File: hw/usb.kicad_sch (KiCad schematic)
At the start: 38 parts, among them J201 USB_C_Receptacle_USB2.0_14P, Q201 CSD18543Q3A, U1001 LMR51430XDDCR, U1002 TPS26750SRSMR, U1003 TPD4S480RUKR, U1004 LMR51430XDDCR, U1005 TPS63700DRCR

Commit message: Checkpoint before resuming project
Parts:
- renumbered C206 to C1001, C208 to C1002, C217 to C1003, C223 to C1004, C224 to C1005, C212 to C1006, C209 to C1007, C213 to C1008, C210 to C1009, C222 to C1010, C214 to C1011, C211 to C1012, C218 to C1013, C219 to C1014, C215 to C1015, C216 to C1016, C220 to C1017, C221 to C1018, J201 to J1001, L1003 to L1001, L1001 to L1003, Q201 to Q1001, R203 to R1001, R202 to R1002, R210 to R1003, R206 to R1004, R207 to R1005, R204 to R1006, R205 to R1007, R208 to R1008, R209 to R1009, U1003 to U1001, U1005 to U1003, U1001 to U1005

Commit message: Working on multi-band BPF and switching
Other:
- company: SoftShack -> WB7NAB
- title: USB connector, ESD, power -> ${title}
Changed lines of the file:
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@@
 	(generator "eeschema")
 	(generator_version "9.0")
-	(paper "A")
+	(paper "USLetter")
 	(title_block
-		(title "USB connector, ESD, power")
-		(date "2025-03-26")
-		(company "SoftShack")
+		(title "${title}")
+		(date "2025-08-10")
+		(company "WB7NAB")
 		(comment 1 "Alan Mimms")
-		(comment 2 "WB7NAB")
 	)
 	(junction

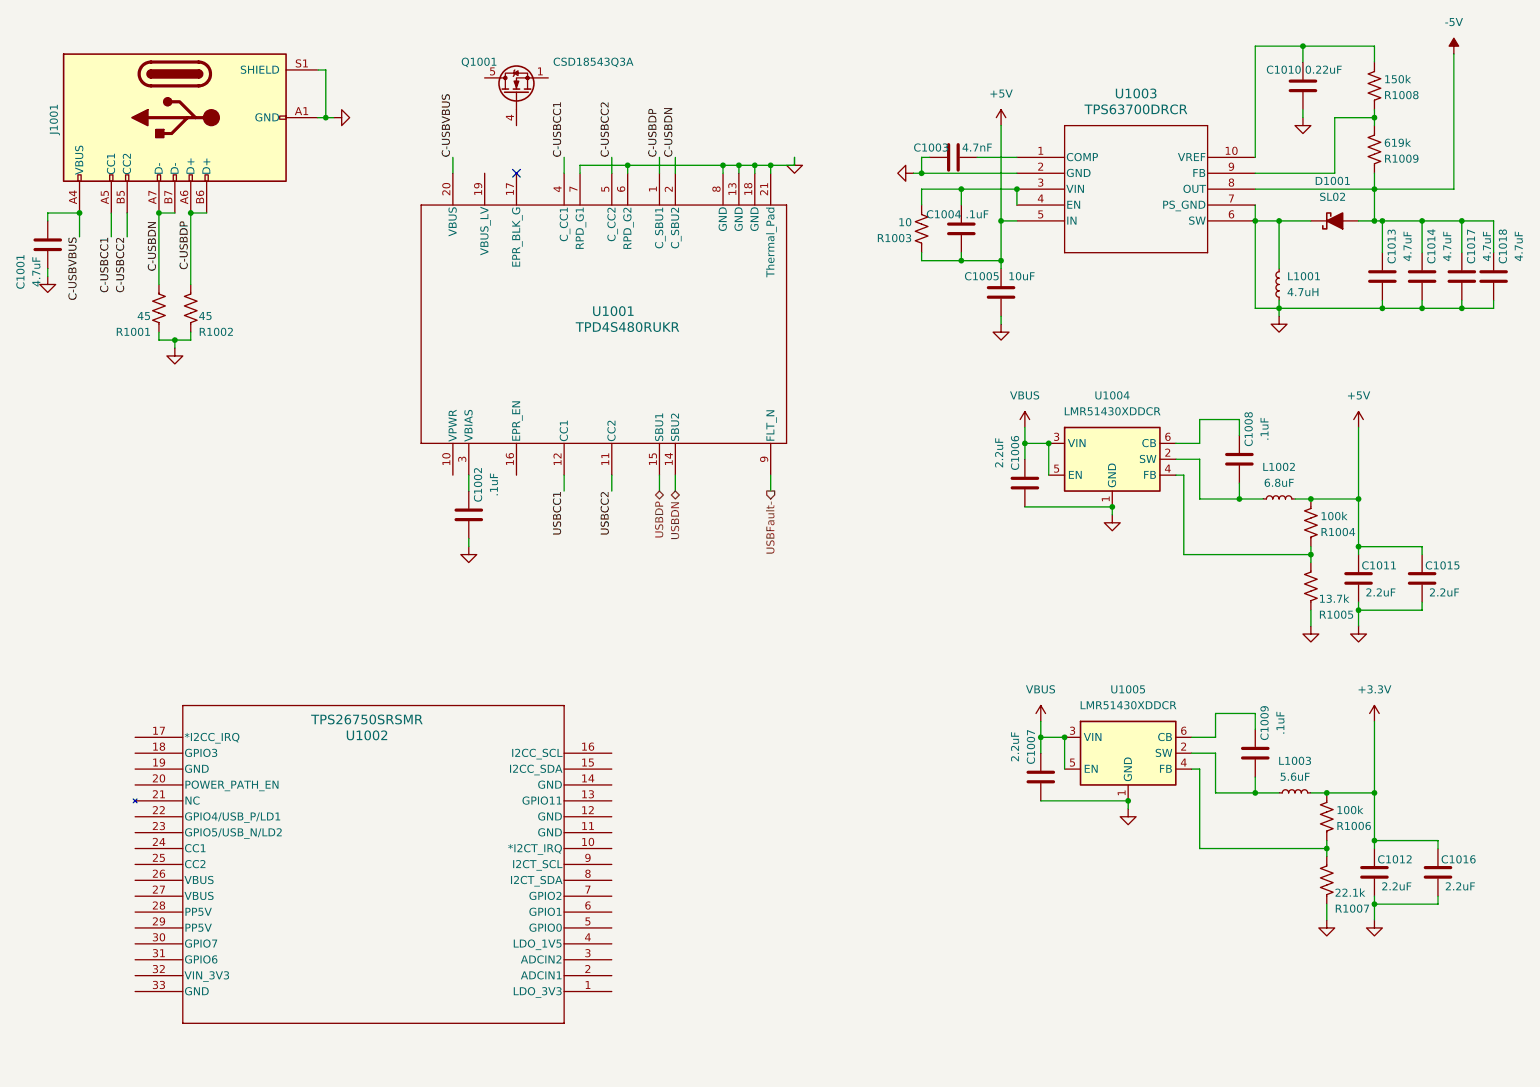
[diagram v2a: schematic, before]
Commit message: Starting to build BPFs for 7 bands
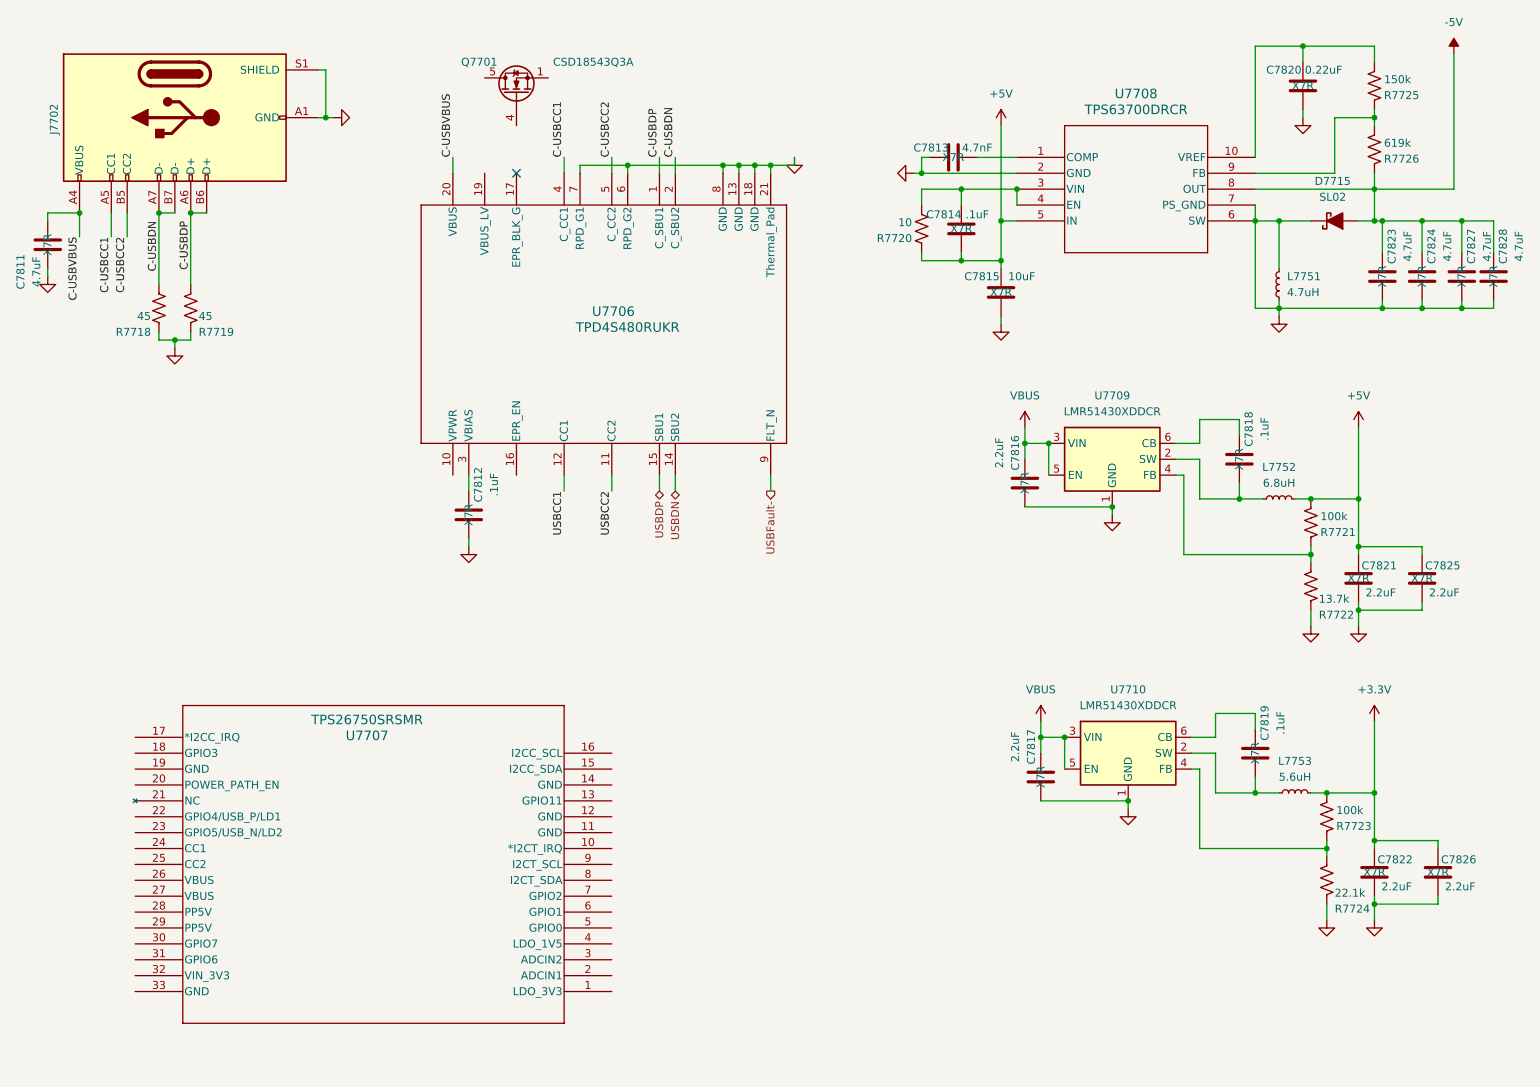
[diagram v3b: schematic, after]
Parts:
- C7811: renamed from C1001; cap-type (none) -> X7R
- C7812: renamed from C1002; cap-type (none) -> X7R
- C7813: renamed from C1003; cap-type (none) -> X7R
- C7814: renamed from C1004; cap-type (none) -> X7R
- C7815: renamed from C1005; cap-type (none) -> X7R
- C7816: renamed from C1006; cap-type (none) -> X7R
- C7817: renamed from C1007; cap-type (none) -> X7R
- C7818: renamed from C1008; cap-type (none) -> X7R
- C7819: renamed from C1009; cap-type (none) -> X7R
- C7820: renamed from C1010; cap-type (none) -> X7R
- C7821: renamed from C1011; cap-type (none) -> X7R
- C7822: renamed from C1012; cap-type (none) -> X7R
- C7823: renamed from C1013; cap-type (none) -> X7R
- C7824: renamed from C1014; cap-type (none) -> X7R
- C7825: renamed from C1015; cap-type (none) -> X7R
- C7826: renamed from C1016; cap-type (none) -> X7R
- C7827: renamed from C1017; cap-type (none) -> X7R
- C7828: renamed from C1018; cap-type (none) -> X7R
- L7752: renamed from L1002; value 6.8uF -> 6.8uH
- L7753: renamed from L1003; value 5.6uF -> 5.6uH
- renumbered D1001 to D7715, J1001 to J7702, L1001 to L7751, Q1001 to Q7701, R1001 to R7718, R1002 to R7719, R1003 to R7720, R1004 to R7721, R1005 to R7722, R1006 to R7723, R1007 to R7724, R1008 to R7725, R1009 to R7726, U1001 to U7706, U1002 to U7707, U1003 to U7708, U1004 to U7709, U1005 to U7710
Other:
- title: ${title} -> USB

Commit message: Getting closer to having all (ten) BPFs designed. Maybe I can try some layout next.
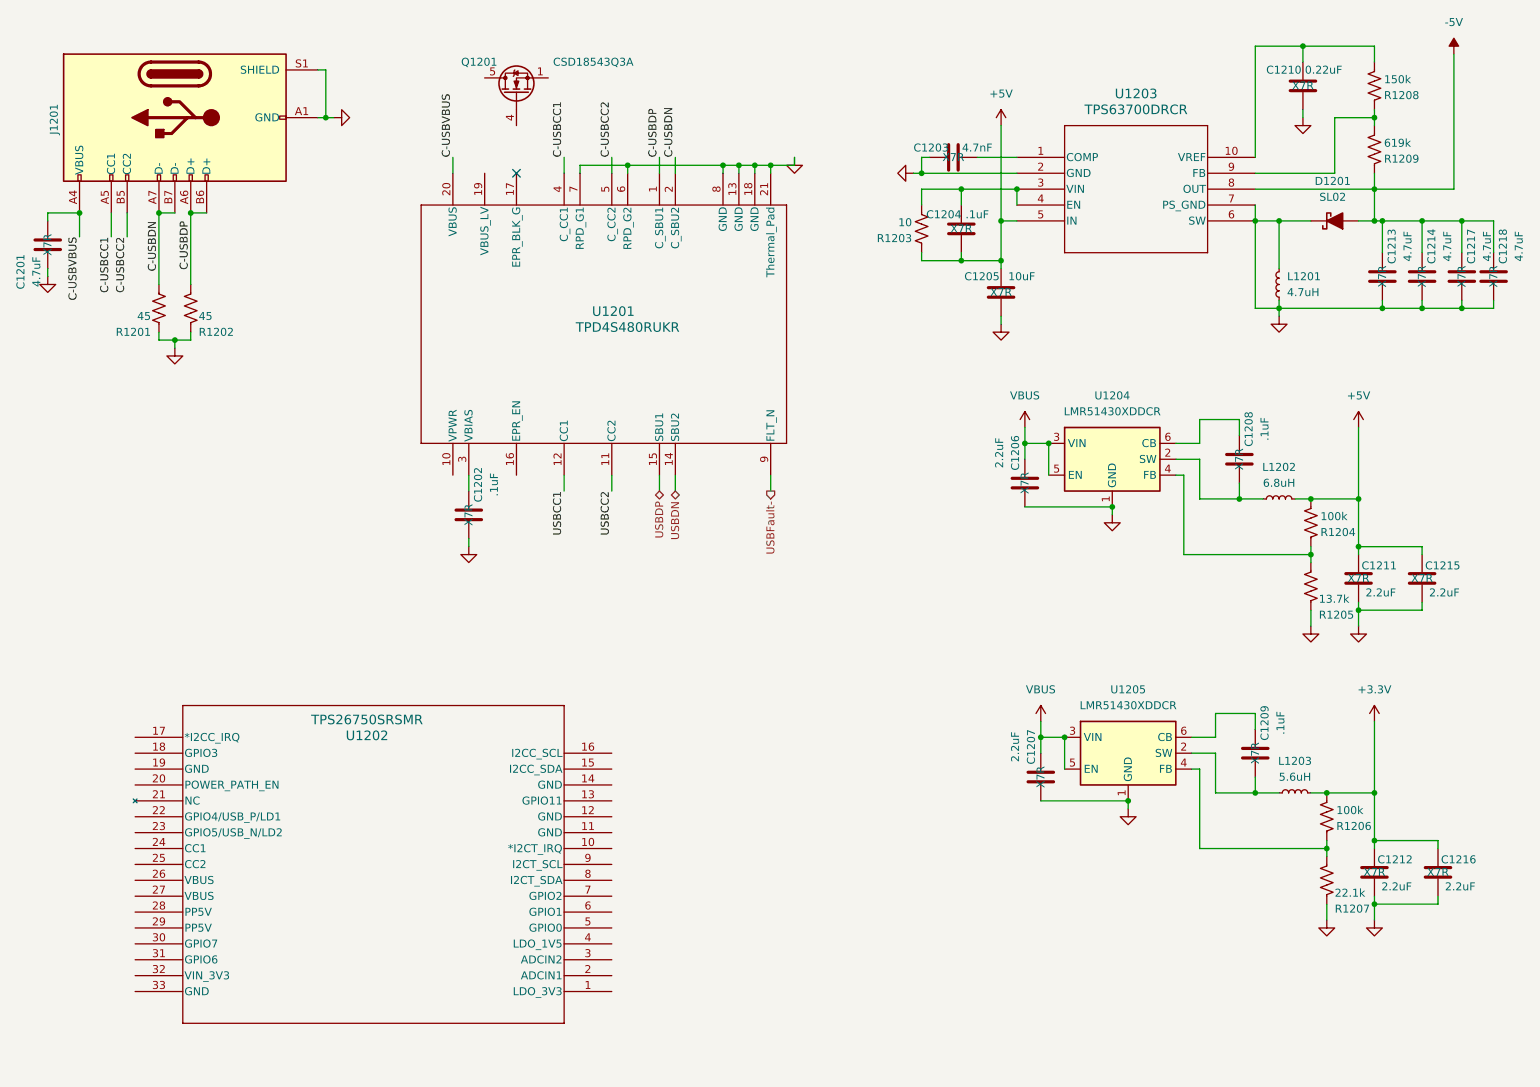
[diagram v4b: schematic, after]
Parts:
- renumbered C7811 to C1201, C7812 to C1202, C7813 to C1203, C7814 to C1204, C7815 to C1205, C7816 to C1206, C7817 to C1207, C7818 to C1208, C7819 to C1209, C7820 to C1210, C7821 to C1211, C7822 to C1212, C7823 to C1213, C7824 to C1214, C7825 to C1215, C7826 to C1216, C7827 to C1217, C7828 to C1218, D7715 to D1201, J7702 to J1201, L7751 to L1201, L7752 to L1202, L7753 to L1203, Q7701 to Q1201, R7718 to R1201, R7719 to R1202, R7720 to R1203, R7721 to R1204, R7722 to R1205, R7723 to R1206, R7724 to R1207, R7725 to R1208, R7726 to R1209, U7706 to U1201, U7707 to U1202, U7708 to U1203, U7709 to U1204, U7710 to U1205

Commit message: Checkpoint hardware. Add README with some notes about software services we need to create.
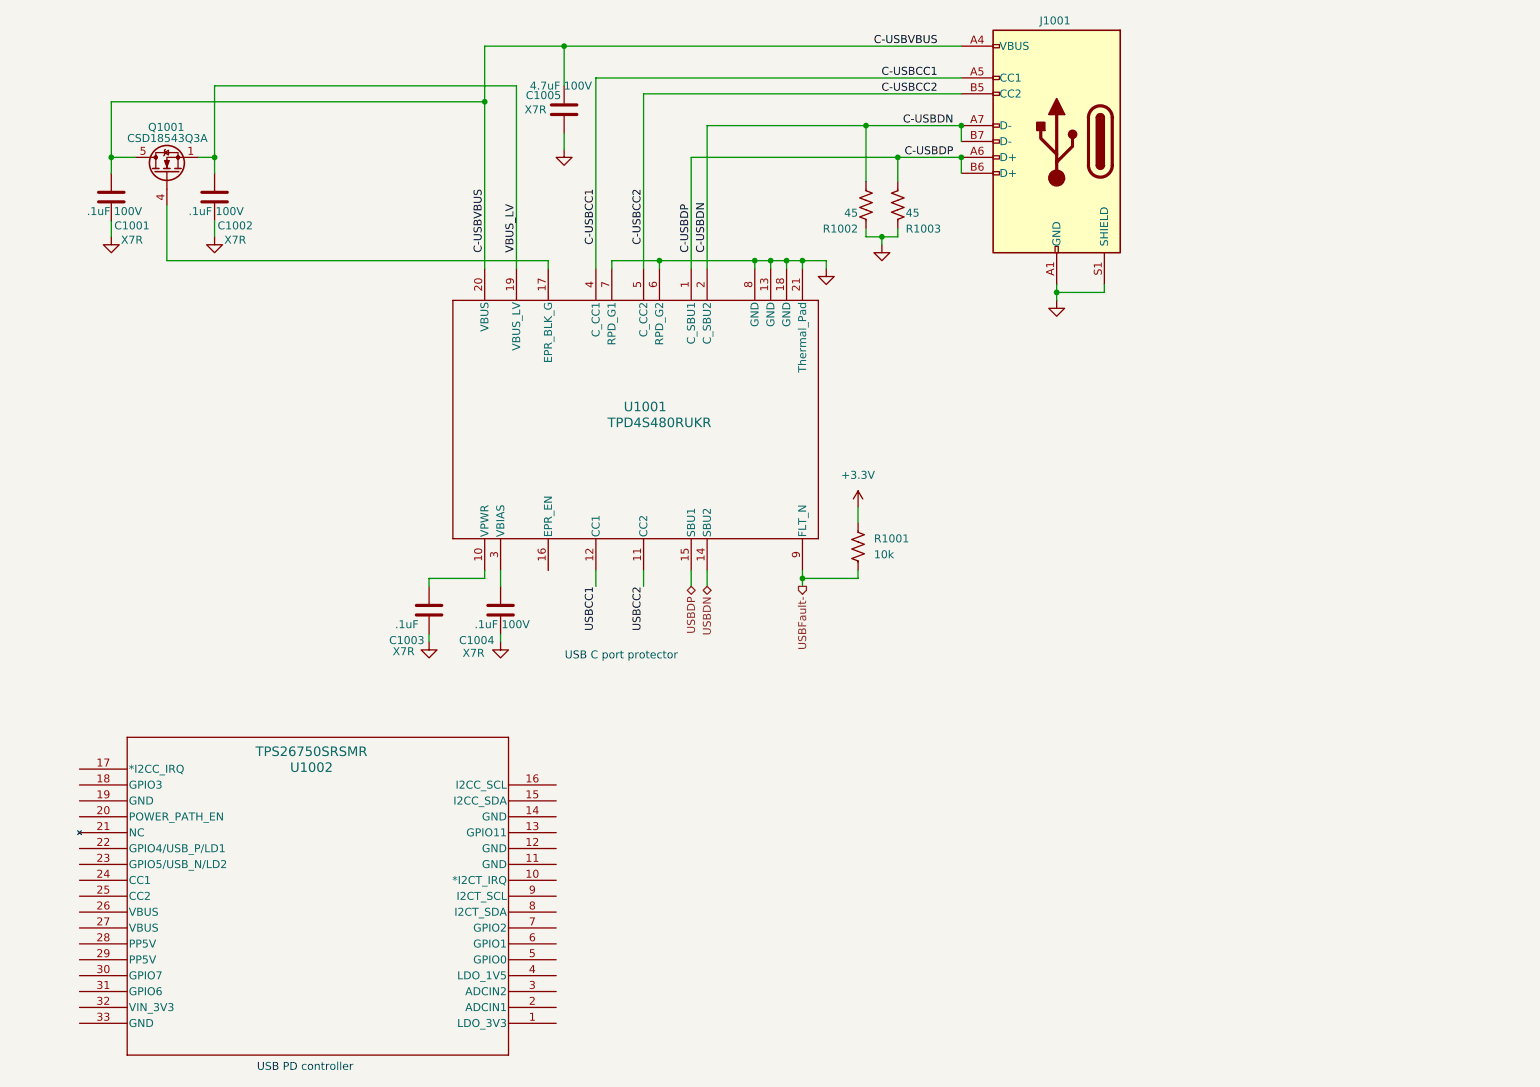
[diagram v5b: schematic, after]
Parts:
- removed C1203: 4.7nF, symbol Device:C
- removed C1204, C1208, C1209: .1uF, symbol Device:C
- removed C1205: 10uF, symbol Device:C
- removed C1206, C1207, C1211, C1212, C1215, C1216: 2.2uF, symbol Device:C
- removed C1210: 0.22uF, symbol Device:C
- removed C1213, C1214, C1217, C1218: 4.7uF, symbol Device:C
- removed D1201: SL02, PCM_Diode_SMD_AKL:D_SMF, symbol PCM_Diode_Schottky_AKL:SL02
- removed L1201: 4.7uH, symbol Device:L_Small
- removed L1202: 6.8uH, symbol Device:L_Small
- removed L1203: 5.6uH, symbol Device:L_Small
- removed R1203: 10, symbol Device:R_US
- removed R1204, R1206: 100k, symbol Device:R_US
- removed R1205: 13.7k, symbol Device:R_US
- removed R1207: 22.1k, symbol Device:R_US
- removed R1208: 150k, symbol Device:R_US
- removed R1209: 619k, symbol Device:R_US
- removed U1203: TPS63700DRCR, DRC10_2P4X1P65, symbol 2025-03-26_20-54-20:TPS63700DRCR
- removed U1204, U1205: LMR51430XDDCR, Package_TO_SOT_SMD:SOT-23-6, symbol Regulator_Switching:LMR51430
- added C1001, C1002: .1uF 100V, symbol Device:C
- added C1003: .1uF, symbol Device:C
- added R1001: 10k, symbol Device:R_US
- C1004: renamed from C1202; value .1uF -> .1uF 100V
- C1005: renamed from C1201; value 4.7uF -> 4.7uF 100V
- renumbered J1201 to J1001, Q1201 to Q1001, R1201 to R1002, R1202 to R1003, U1201 to U1001, U1202 to U1002
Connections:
- net +3.3V: now also R1001.1
- net C-USBVBUS: now also Q1001.5 (D), C1001.1
- net GND: now also C1001.2, C1002.2, C1003.2
- net USBFault-: now also R1001.2
- net at U1001.10 (VPWR): now also C1003.1
- net at U1001.17 (EPR_BLK_G): now also Q1001.4 (G)
- net VBUS_LV: now reaches U1001.19 (VBUS_LV)
- net VBUS_LV: now also Q1001.1 (S), Q1001.2 (S), Q1001.3 (S), C1002.1
- no-connect marks 1 -> 0
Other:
- note added: "USB C port protector"
- note added: "USB PD controller"
- moved on the sheet: C1004, C1005, J1001, Q1001, R1002, R1003, U1001, U1002
